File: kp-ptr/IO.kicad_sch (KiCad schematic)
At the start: 27 parts, among them J6 Conn_01x06_Male, J7 Conn_01x10_Male, J8 Conn_01x06_Male, J9 Conn_01x02_Male, Q1 NMOS_SOT23

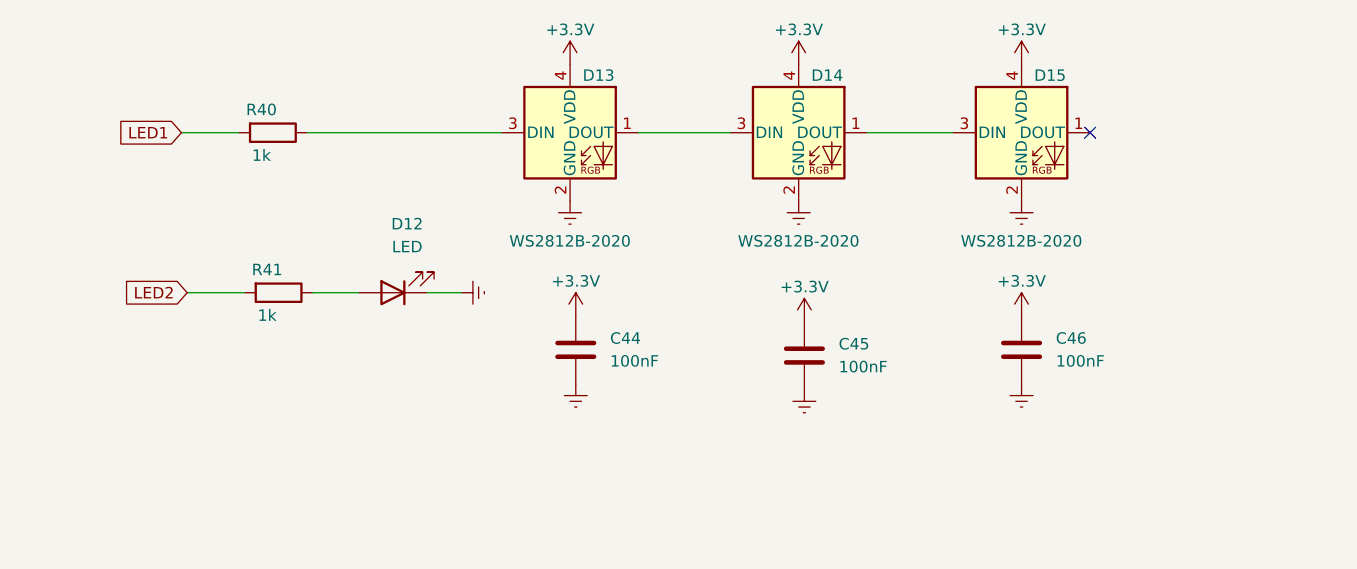
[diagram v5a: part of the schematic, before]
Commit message: Second LSM added
Both LSM has INT connected
Small pins changes
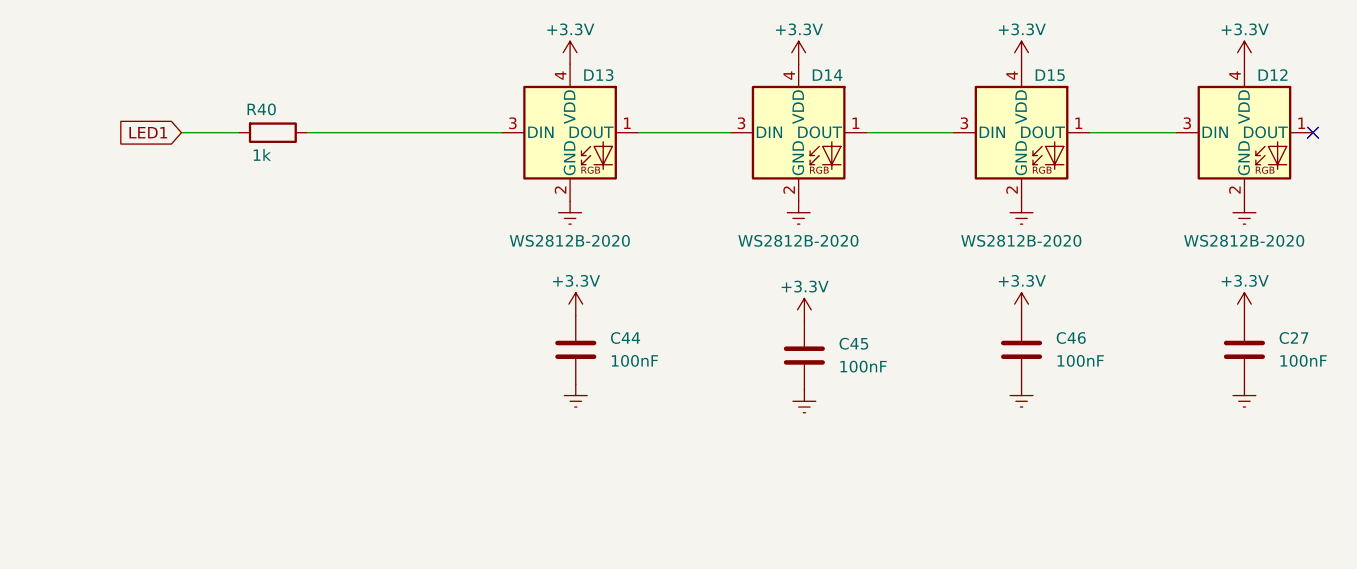
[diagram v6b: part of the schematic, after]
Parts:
- removed D12: LED, LED_SMD:LED_0603_1608Metric, symbol Device:LED
- removed R41: 1k, Resistor_SMD:R_0402_1005Metric, symbol Device:R
- added C27: 100nF, Capacitor_SMD:C_0402_1005Metric, symbol Device:C
- added D12: WS2812B-2020, KP-PTR_lib:WS2812B-2020, symbol KP-PTR_lib:WS2812B-2020
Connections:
- net +3V3: now also C27.1, D12.4 (VDD)
- net Earth: now also C27.2, D12.2 (GND)
- net at D15.1 (DOUT): now also D12.3 (DIN)
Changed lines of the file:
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@@
   (junction (at 55.88 88.9) (diameter 0) (color 0 0 0 0)
   )
-  (no_connect (at 140.97 29.21))
+  (no_connect (at 165.735 29.21))
   (wire (pts (xy 66.04 159.385) (xy 66.04 154.305))
     (stroke (width 0) (type default) (color 0 0 0 0))
@@
     (stroke (width 0) (type default) (color 0 0 0 0))
   )
+  (wire (pts (xy 140.97 29.21) (xy 150.495 29.21))
+    (stroke (width 0) (type default) (color 0 0 0 0))
+  )
   (wire (pts (xy 40.005 29.21) (xy 46.355 29.21))
     (stroke (width 0) (type default) (color 0 0 0 0))
@@
     (stroke (width 0) (type default) (color 0 0 0 0))
   )
-  (wire (pts (xy 71.12 46.99) (xy 67.31 46.99))
-    (stroke (width 0) (type default) (color 0 0 0 0))
-  )
   (wire (pts (xy 44.45 107.95) (xy 48.26 107.95))
     (stroke (width 0) (type default) (color 0 0 0 0))
@@
     (stroke (width 0) (type default) (color 0 0 0 0))
   )
-  (wire (pts (xy 40.64 46.99) (xy 46.99 46.99))
-    (stroke (width 0) (type default) (color 0 0 0 0))
-  )
   (wire (pts (xy 82.55 187.96) (xy 85.09 187.96))
     (stroke (width 0) (type default) (color 0 0 0 0))
@@
   )
   (wire (pts (xy 36.83 139.065) (xy 45.085 139.065))
-    (stroke (width 0) (type default) (color 0 0 0 0))
-  )
-  (wire (pts (xy 54.61 46.99) (xy 59.69 46.99))
     (stroke (width 0) (type default) (color 0 0 0 0))
   )
@@
     (effects (font (size 1.27 1.27)) (justify right))
     (property "Intersheet References" "${INTERSHEET_REFS}" (id 0) (at 28.7624 185.3406 0)
-      (effects (font (size 1.27 1.27)) (justify right) hide)
-    )
-  )
-  (global_label "LED2" (shape input) (at 40.64 46.99 180) (fields_autoplaced)
-    (effects (font (size 1.27 1.27)) (justify right))
-    (property "Intersheet References" "${INTERSHEET_REFS}" (id 0) (at 33.5702 46.9106 0)
       (effects (font (size 1.27 1.27)) (justify right) hide)
     )
@@
     (pin "1")
     (pin "2")
-  )
-  (symbol (lib_id "power:Earth") (at 71.12 46.99 90) (unit 1)
-    (in_bom yes) (on_board yes) (fields_autoplaced)
-    (property "Reference" "#PWR0143" (id 0) (at 77.47 46.99 0)
-      (effects (font (size 1.27 1.27)) hide)
-    )
-    (property "Value" "Earth" (id 1) (at 74.93 46.99 0)
-      (effects (font (size 1.27 1.27)) hide)
-    )
-    (property "Footprint" "" (id 2) (at 71.12 46.99 0)
-      (effects (font (size 1.27 1.27)) hide)
-    )
-    (property "Datasheet" "~" (id 3) (at 71.12 46.99 0)
-      (effects (font (size 1.27 1.27)) hide)
-    )
-    (pin "1")
   )
   (symbol (lib_id "power:Earth") (at 40.005 190.5 0) (unit 1)
@@
     (pin "4")
   )
-  (symbol (lib_id "Device:LED") (at 63.5 46.99 180) (unit 1)
-    (in_bom yes) (on_board yes) (fields_autoplaced)
-    (property "Reference" "D12" (id 0) (at 65.0875 39.37 0))
-    (property "Value" "LED" (id 1) (at 65.0875 41.91 0))
-    (property "Footprint" "LED_SMD:LED_0603_1608Metric" (id 2) (at 63.5 46.99 0)
-      (effects (font (size 1.27 1.27)) hide)
-    )
-    (property "Datasheet" "~" (id 3) (at 63.5 46.99 0)
-      (effects (font (size 1.27 1.27)) hide)
-    )
-    (pin "1")
-    (pin "2")
-  )
   (symbol (lib_id "Device:R") (at 113.03 154.94 180) (unit 1)
     (in_bom yes) (on_board yes)
@@
     (pin "2")
   )
+  (symbol (lib_id "power:Earth") (at 158.115 57.15 0) (unit 1)
+    (in_bom yes) (on_board yes) (fields_autoplaced)
+    (property "Reference" "#PWR0143" (id 0) (at 158.115 63.5 0)
+      (effects (font (size 1.27 1.27)) hide)
+    )
+    (property "Value" "Earth" (id 1) (at 158.115 60.96 0)
+      (effects (font (size 1.27 1.27)) hide)
+    )
+    (property "Footprint" "" (id 2) (at 158.115 57.15 0)
+      (effects (font (size 1.27 1.27)) hide)
+    )
+    (property "Datasheet" "~" (id 3) (at 158.115 57.15 0)
+      (effects (font (size 1.27 1.27)) hide)
+    )
+    (pin "1")
+  )
   (symbol (lib_id "Transistor_FET:IRLML2060") (at 53.34 107.95 0) (unit 1)
     (in_bom yes) (on_board yes) (fields_autoplaced)
@@
     (pin "2")
   )
-  (symbol (lib_id "Device:R") (at 50.8 46.99 270) (unit 1)
-    (in_bom yes) (on_board yes)
-    (property "Reference" "R41" (id 0) (at 49.53 44.45 90))
-    (property "Value" "1k" (id 1) (at 49.53 49.53 90))
-    (property "Footprint" "Resistor_SMD:R_0402_1005Metric" (id 2) (at 50.8 45.212 90)
-      (effects (font (size 1.27 1.27)) hide)
-    )
-    (property "Datasheet" "~" (id 3) (at 50.8 46.99 0)
-      (effects (font (size 1.27 1.27)) hide)
-    )
-    (pin "1")
-    (pin "2")
+  (symbol (lib_id "power:Earth") (at 158.115 36.83 0) (unit 1)
+    (in_bom yes) (on_board yes) (fields_autoplaced)
+    (property "Reference" "#PWR095" (id 0) (at 158.115 43.18 0)
+      (effects (font (size 1.27 1.27)) hide)
+    )
+    (property "Value" "Earth" (id 1) (at 158.115 40.64 0)
+      (effects (font (size 1.27 1.27)) hide)
+    )
+    (property "Footprint" "" (id 2) (at 158.115 36.83 0)
+      (effects (font (size 1.27 1.27)) hide)
+    )
+    (property "Datasheet" "~" (id 3) (at 158.115 36.83 0)
+      (effects (font (size 1.27 1.27)) hide)
+    )
+    (pin "1")
   )
   (symbol (lib_id "Diode:1N4148") (at 49.53 95.25 270) (unit 1)
@@
     (pin "4")
   )
+  (symbol (lib_id "power:+3.3V") (at 158.115 49.53 0) (unit 1)
+    (in_bom yes) (on_board yes)
+    (property "Reference" "#PWR0113" (id 0) (at 158.115 53.34 0)
+      (effects (font (size 1.27 1.27)) hide)
+    )
+    (property "Value" "+3.3V" (id 1) (at 158.115 45.72 0))
+    (property "Footprint" "" (id 2) (at 158.115 49.53 0)
+      (effects (font (size 1.27 1.27)) hide)
+    )
+    (property "Datasheet" "" (id 3) (at 158.115 49.53 0)
+      (effects (font (size 1.27 1.27)) hide)
+    )
+    (pin "1")
+  )
   (symbol (lib_id "power:Earth") (at 59.69 159.385 0) (unit 1)
     (in_bom yes) (on_board yes) (fields_autoplaced)
@@
     (pin "1")
     (pin "2")
+  )
+  (symbol (lib_id "Device:C") (at 158.115 53.34 0) (unit 1)
+    (in_bom yes) (on_board yes) (fields_autoplaced)
+    (property "Reference" "C27" (id 0) (at 161.925 52.0699 0)
+      (effects (font (size 1.27 1.27)) (justify left))
+    )
+    (property "Value" "100nF" (id 1) (at 161.925 54.6099 0)
+      (effects (font (size 1.27 1.27)) (justify left))
+    )
+    (property "Footprint" "Capacitor_SMD:C_0402_1005Metric" (id 2) (at 159.0802 57.15 0)
+      (effects (font (size 1.27 1.27)) hide)
+    )
+    (property "Datasheet" "~" (id 3) (at 158.115 53.34 0)
+      (effects (font (size 1.27 1.27)) hide)
+    )
+    (pin "1")
+    (pin "2")
+  )
+  (symbol (lib_id "power:+3.3V") (at 158.115 21.59 0) (unit 1)
+    (in_bom yes) (on_board yes)
+    (property "Reference" "#PWR01" (id 0) (at 158.115 25.4 0)
+      (effects (font (size 1.27 1.27)) hide)
+    )
+    (property "Value" "+3.3V" (id 1) (at 158.115 17.78 0))
+    (property "Footprint" "" (id 2) (at 158.115 21.59 0)
+      (effects (font (size 1.27 1.27)) hide)
+    )
+    (property "Datasheet" "" (id 3) (at 158.115 21.59 0)
+      (effects (font (size 1.27 1.27)) hide)
+    )
+    (pin "1")
   )
   (symbol (lib_id "power:Earth") (at 55.88 115.57 0) (unit 1)
@@
     (pin "2")
   )
+  (symbol (lib_id "KP-PTR_lib:WS2812B-2020") (at 158.115 29.21 0) (unit 1)
+    (in_bom yes) (on_board yes)
+    (property "Reference" "D12" (id 0) (at 161.29 22.86 0))
+    (property "Value" "WS2812B-2020" (id 1) (at 158.115 41.275 0))
+    (property "Footprint" "KP-PTR_lib:WS2812B-2020" (id 2) (at 159.385 36.83 0)
+      (effects (font (size 1.27 1.27)) (justify left top) hide)
+    )
+    (property "Datasheet" "https://www.tme.eu/Document/8b264124130de6e17f8ce807c3210601/WS2812B-2020.pdf" (id 3) (at 160.655 38.735 0)
+      (effects (font (size 1.27 1.27)) (justify left top) hide)
+    )
+    (pin "1")
+    (pin "2")
+    (pin "3")
+    (pin "4")
+  )
   (symbol (lib_id "KP-PTR_lib:WS2812B-2020") (at 83.185 29.21 0) (unit 1)

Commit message: Igniters rework
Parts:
- Q1: footprint Package_TO_SOT_SMD:SOT-23 -> KP-PTR_lib:SOT-23
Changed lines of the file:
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@@
       (effects (font (size 1.27 1.27)) (justify left))
     )
-    (property "Footprint" "Package_TO_SOT_SMD:SOT-23" (id 2) (at 58.42 109.855 0)
+    (property "Footprint" "KP-PTR_lib:SOT-23" (id 2) (at 58.42 109.855 0)
       (effects (font (size 1.27 1.27) italic) (justify left) hide)
     )
